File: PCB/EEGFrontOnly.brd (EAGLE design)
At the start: 160 x 100 mm, 95 parts, among them IC1 ADS1299-X, IC2 ADUM3151-3, IC3 HT7333, J2 USB_B_PTH, U1 LP2985-33DBVT, U2 B0505S-1WB0505S-1W, U3 TPS60403DBVT, U4 TPS73225DBVR, U5 TPS73225DBVR, U6 TPD4E1B06DCKR, U7 TPD4E1B06DCKR, U8 TPD4E1B06DCKR

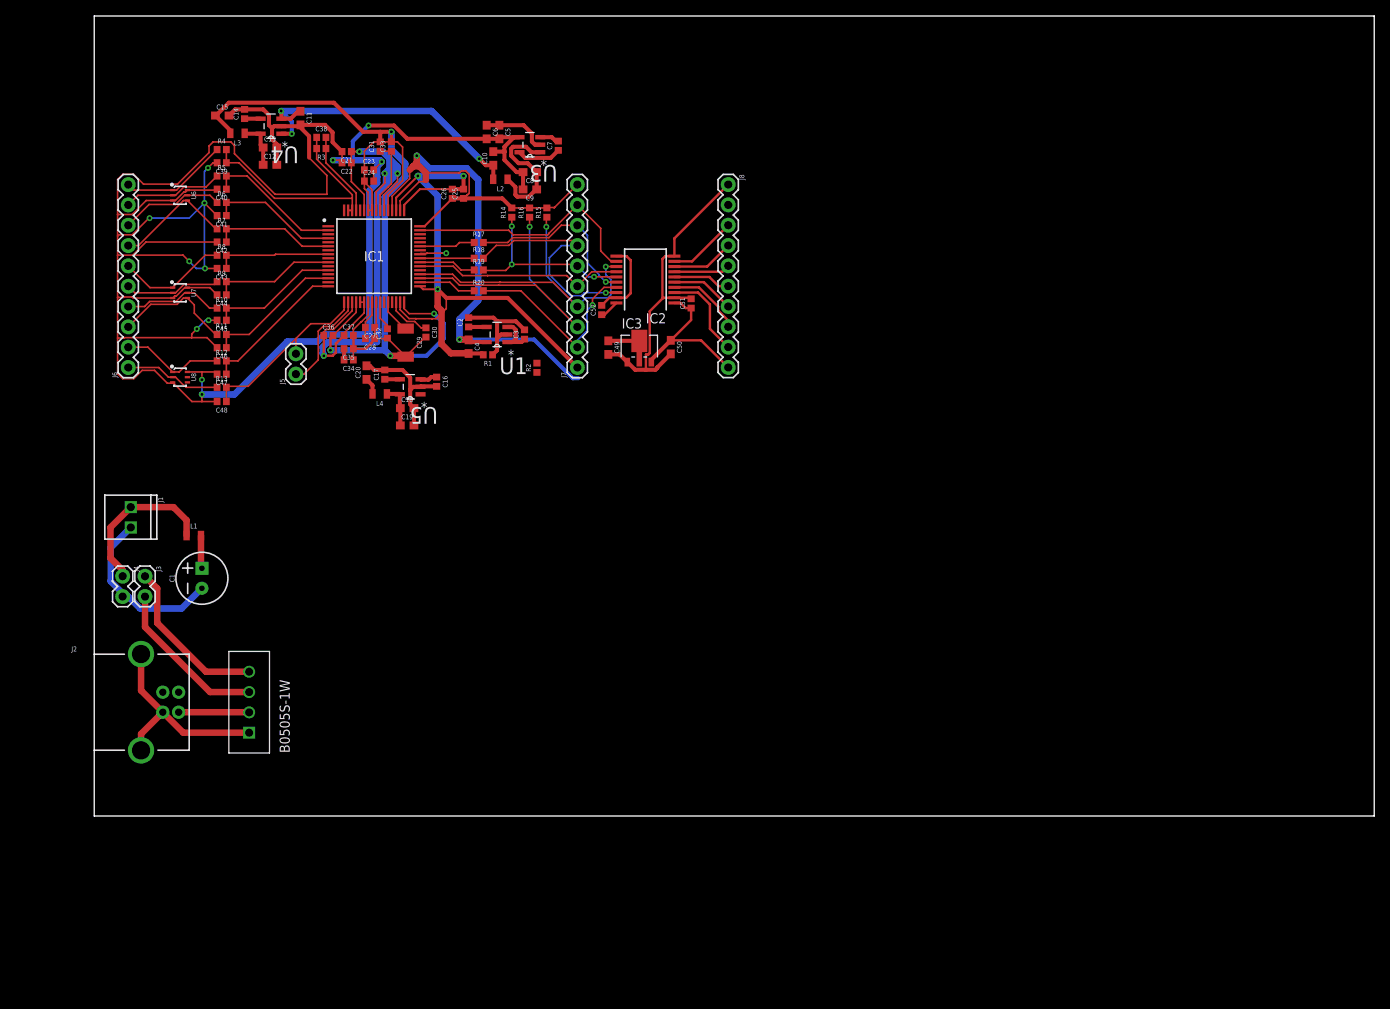
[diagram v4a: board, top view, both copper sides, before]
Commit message: PCB wiring complete
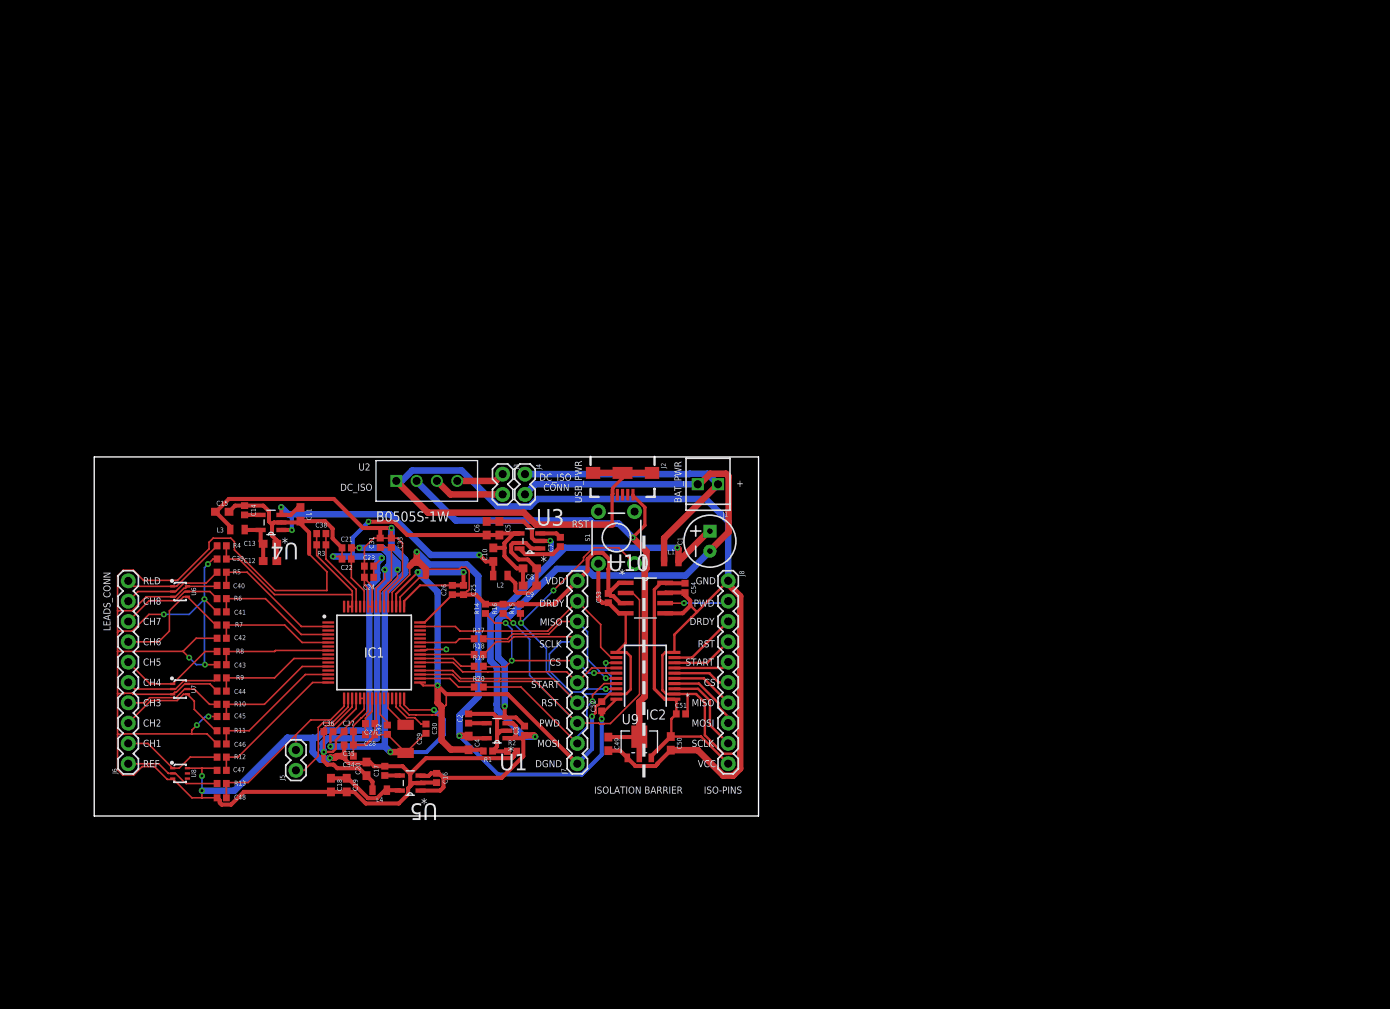
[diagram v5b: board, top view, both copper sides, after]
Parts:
- removed IC3: HT7333, holtek2:SOT-89
- added C53, C54: 0.1uF, SparkFun-Capacitors:0402
- added S1: MOMENTARY-SWITCH-SPST-PTH-6.0MM, SparkFun-Switches:TACTILE_SWITCH_PTH_6.0MM
- added U10: ISO721D, Texas Instruments_By_element14_Batch_1:SOIC127P600X175-8N
- added U9: HT7333, holtek2:SOT-89
- J2: value USB_B_PTH -> (none); device SparkFun-Connectors:USB-B-PTH -> SparkFun-Connectors:USB-B-MICRO-SMD_RED_PASTE
- moved J1 73.5 mm to (78.0, 41.5), turned to 180 degrees
- moved J2 67.8 mm to (66.0, 42.9), turned to 270 degrees
- moved C1 63.7 mm to (77.0, 34.4)
- moved L1 59.8 mm to (72.1, 31.8)
- moved J4 51.9 mm to (53.8, 42.7)
- moved C51 51.3 mm to (73.3, 12.8), turned to 0 degrees
- moved R14 49.6 mm to (48.9, 25.9)
- moved R15 49.6 mm to (53.3, 25.9)
- moved R16 49.6 mm to (51.1, 25.9)
- moved C7 49.5 mm to (58.3, 34.3)
- moved C14 49.5 mm to (18.8, 38.2)
- moved C15 49.5 mm to (16.0, 38.0)
- moved C5 49.5 mm to (50.6, 36.0)
- moved C6 49.5 mm to (49.1, 36.0)
- moved R17 49.5 mm to (48.1, 22.2)
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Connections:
- removed net SPI_PWD: J8.2
- new net ISO_PWD: J8.2, U10.6
- net DGND: now also C53.2, S1.1, U10.4
- net DVDD: now also C53.1, U10.1, U10.3
- net GND-ISO: now also C54.2, J2.SHIELD1, J2.SHIELD2, J2.SHIELD3, U10.5, U10.7, U9.2; no longer IC3.2, J2.SHLD1, J2.SHLD2
- net PWD: now also U10.2
- net RST: now also S1.3
- net VCC-ISO: now also U9.3, U9.4; no longer IC3.3, IC3.4
- net VCCIO: now also C54.1, U10.8, U9.1; no longer IC3.1
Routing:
- net GND-ISO: track 67.6 -> 184.4 mm
- net VBAT: track 19.7 -> 92.4 mm, vias 0 -> 3
- net GND: track 35.4 -> 95.7 mm, vias 0 -> 1
- net VCC-ISO: track 15.0 -> 68.8 mm, vias 0 -> 1
- net AGND: track 321.0 -> 361.7 mm, vias 12 -> 13
- net DVDD: track 101.5 -> 127.1 mm, vias 2 -> 3
- net PWD: track 38.4 -> 63.0 mm
- net DGND: track 97.4 -> 120.5 mm, vias 4 -> 5
- net RST: track 44.2 -> 64.6 mm, vias 2 -> 3
- net VBATPRE: track 19.9 -> 37.1 mm
- net VCCIO: track 19.8 -> 37.0 mm
- net N$1: track 20.5 -> 6.03 mm
- net N$2: track 20.2 -> 8.92 mm
- net ISO_PWD: track 0.00 -> 7.99 mm, vias 0 -> 1
- net AVDD: track 83.3 -> 90.5 mm
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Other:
- board size 160 x 100 mm -> 83 x 44.9 mm
- board text added: "*"
- board text added: "+"
- board text added: "BAT_PWR"
- board text added: "CH1"
- board text added: "CH2"
- board text added: "CH3"
- board text added: "CH4"
- board text added: "CH5"
- board text added: "CH6"
- board text added: "CH7"
- board text added: "CH8"
- board text added: "CONN"
- board text added: "CS"
- board text added: "DC_ISO"
- board text added: "DGND"
- board text added: "DRDY"
- board text added: "GND"
- board text added: "ISO-PINS"
- board text added: "ISOLATION BARRIER"
- board text added: "LEADS_CONN"
- board text added: "MISO"
- board text added: "MOSI"
- board text added: "PWD"
- board text added: "REF"
- board text added: "RLD"
- board text added: "RST"
- board text added: "SCLK"
- board text added: "START"
- board text added: "U2"
- board text added: "USB_PWR"
- board text added: "VCC"
- board text added: "VDD"

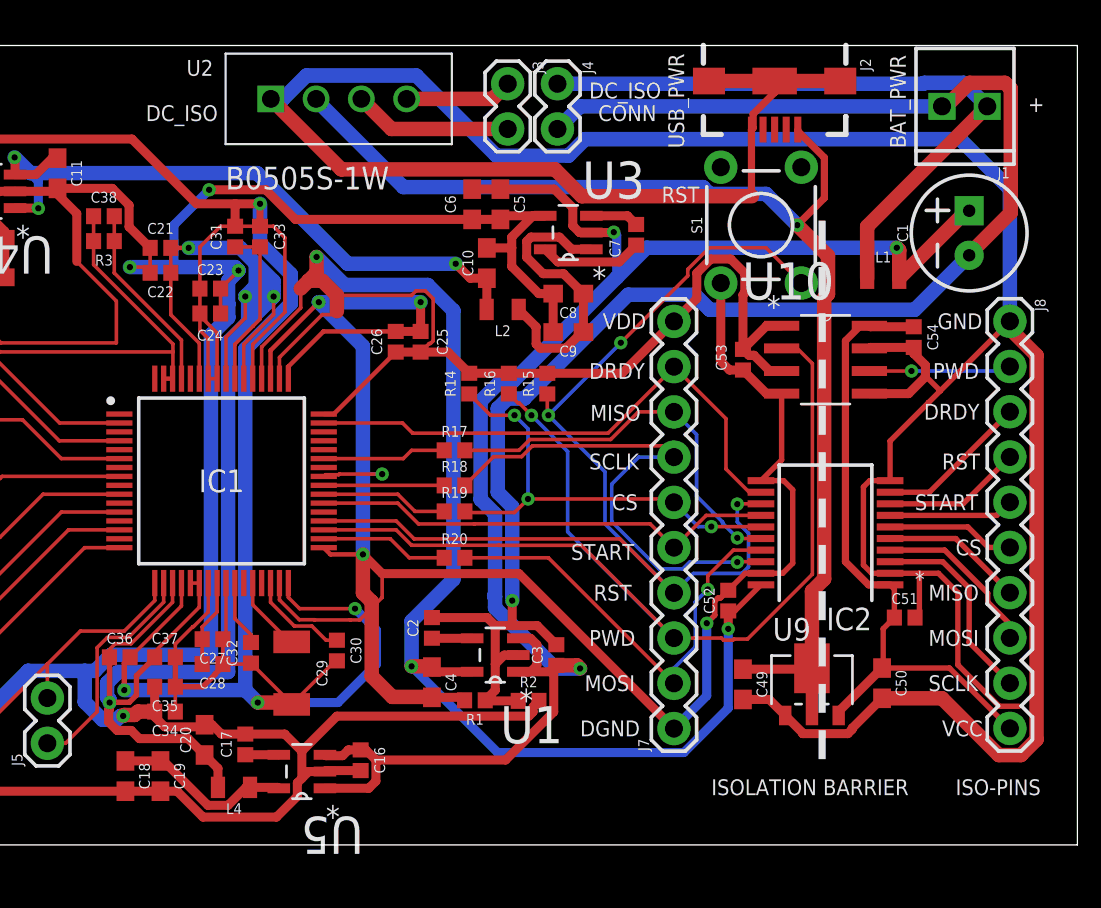
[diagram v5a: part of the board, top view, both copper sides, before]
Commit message: text adjusting & add power pins and less
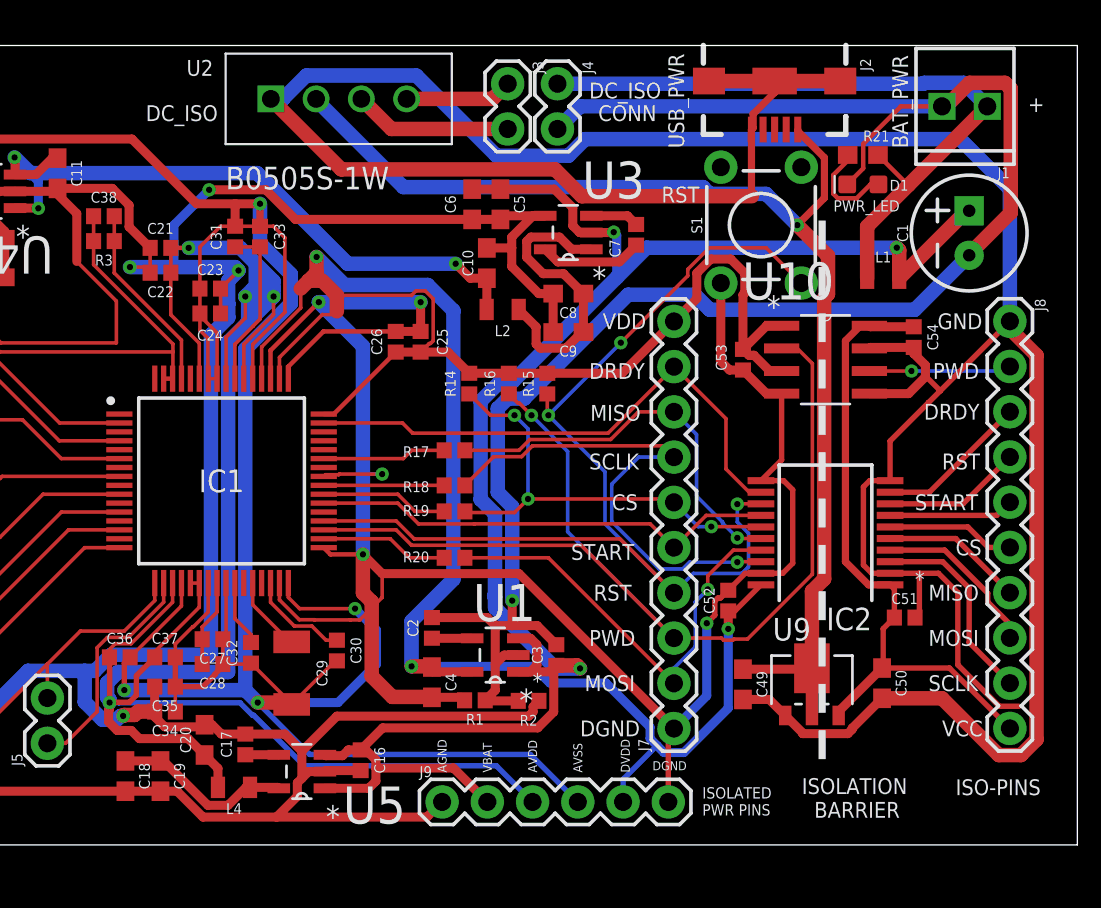
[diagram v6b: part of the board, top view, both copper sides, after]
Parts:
- added D1: GREEN, SparkFun-LED:LED-0603
- added J9: (no value), SparkFun-Connectors:1X06
- added R21: 2.2k, SparkFun-Resistors:0603
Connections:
- new net N$27: D1.A, R21.1
- net AGND: now also J9.1
- net AVDD: now also J9.3
- net AVSS: now also J9.4
- net DGND: now also J9.6
- net DVDD: now also J9.5
- net GND: now also D1.C
- net VBAT: now also J9.2
- net VBATPRE: now also R21.2
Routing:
- net AVDD: track 90.5 -> 116.6 mm
- net AVSS: track 142.4 -> 162.7 mm
- net AGND: track 361.7 -> 371.3 mm
- net GND: track 95.7 -> 103.6 mm
- net VBAT: track 92.4 -> 100.0 mm
- net N$27: track 0.00 -> 5.47 mm
- net DVDD: track 127.1 -> 131.5 mm
- net DGND: track 120.5 -> 124.7 mm
- net VBATPRE: track 37.1 -> 39.6 mm
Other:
- board text added: "AGND"
- board text added: "AVDD"
- board text added: "AVSS"
- board text added: "DVDD"
- board text added: "ISOLATED PWR PINS"
- board text added: "PWR_LED"
- board text added: "VBAT"

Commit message: front only PCB complete!
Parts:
- added J10: (no value), SparkFun-Connectors:1X02
- added U$3, U$5, U$6, U$7: (no value), SparkFun-Hardware:STAND-OFF
- moved C1 1.78 mm to (77.0, 36.1)
- moved U2 1.78 mm to (37.8, 43.7)
- moved C12 1.78 mm to (22.0, 33.6)
- moved C25 1.78 mm to (46.2, 30.0)
- moved C26 1.78 mm to (44.8, 30.0)
- moved C40 1.78 mm to (15.9, 30.6)
- moved C41 1.78 mm to (15.9, 27.3)
- moved C53 1.78 mm to (64.3, 29.0)
- moved C9 1.78 mm to (54.5, 30.6)
- moved L1 1.78 mm to (72.1, 33.6)
- moved L2 1.78 mm to (50.8, 31.8)
- moved R17 1.78 mm to (48.1, 23.9)
- moved R6 1.78 mm to (15.9, 28.9)
- moved U10 1.78 mm to (68.9, 29.0)
- moved U6 1.78 mm to (10.7, 29.8)
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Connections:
- net P_BIAS: now also J10.2
- net P_IN8: now also J10.1
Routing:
- net P_IN8: track 12.6 -> 21.7 mm
- net P_BIAS: track 13.5 -> 20.1 mm
- added copper zone on layer 1, net AGND
- added copper zone on layer 16, net AGND
- added copper zone on layer 1, net DGND
- added copper zone on layer 16, net DGND
- added copper zone on layer 1, net GND-ISO
- added copper zone on layer 16, net GND-ISO
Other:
- board size 83 x 44.9 mm -> 87.5 x 46.7 mm
- board text added: "ADS1299-IPAGR"
- board text added: "EEG-FrontOnly PCB"
- board text added: "Jingjie Li - 25 MAR 2019"
- board text added: "RLD-CH8"
